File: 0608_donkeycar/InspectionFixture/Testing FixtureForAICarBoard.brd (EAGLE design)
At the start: 65 x 56.5 mm, 89 parts, among them CON1 RASPBERRYPI_SHEILD

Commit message: AI Car Board テスト治具 Rev1.0.0 アルファ版　完成
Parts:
- removed U$1: RP2350A, FaBo-MPU:QFN60
- removed U$10: MLP2520S2R2MT0S1, FaBo-Coil:1008(2520MM)
- removed U$11: DMG1012T, FaBo-Mosfet:SOT-523
- removed U$12, U$14: TS-06104, FaBo-Switch:TS-06104
- removed U$13: MCP3008, FaBo-ADC:SOIC-16
- removed U$2: W25Q32RVXHJQ, FaBo-NORFLASH:XSON8
- removed U$3: ABM8-272-T3, FaBo-Crystal:ABM8-272-T3
- removed U$5: TXB0104, FaBo-LevelTranslator:TSSOP-14
- removed U$6: PMEG6010ELR-Q, FaBo-Diode:SOD123W
- removed U$7: 5077CR-16-SMC2-BK-TR, FaBo-USB:5077CR-16-SMC2-BK-TR
- removed U$8: RT6150B-33GQW, FaBo-Supply:WDFN-10L_2.5X2.5MM
- removed U$9: AOTA-B201610S3R3-101-T, FaBo-Coil:0806(2016MM)
- added BT1, BT2: TS-06104, FaBo-Switch:TS-06104
- added C33: 0.1uF, FaBo-Capacitor:0603-BOTTOM
- added CN2, CN3, CN4, CN5, CN6: (no value), FaBo-PIN:PIN_1X1_SMALL
- added CON2: 5077CR-16-SMC2-BK-TR, FaBo-USB:5077CR-16-SMC2-BK-TR
- added D2, D3: PMEG6010ELR-Q, FaBo-Diode:SOD123W
- added L1: MLP2520S2R2MT0S1, FaBo-Coil:1008(2520MM)
- added L2: AOTA-B201610S3R3-101-T, FaBo-Coil:0806(2016MM)
- added LED2: (no value), FaBo-LED:WS2812B_NARROW
- added OSC: ABM8-272-T3, FaBo-Crystal:ABM8-272-T3
- added R38: 100K, FaBo-Resistors:0603
- added R39: DNP, FaBo-Resistors:0603-BOTTOM
- added U1: RP2350A, FaBo-MPU:QFN60
- added U3: TXB0104, FaBo-LevelTranslator:TSSOP-14
- added U4: RT6150B-33GQW, FaBo-Supply:WDFN-10L_2.5X2.5MM
- added U5: DMG1012T, FaBo-Mosfet:SOT-523
- added U6: MCP3008, FaBo-ADC:SOIC-16
- added U7: (no value), FaBo-Display:ER-CON30HT-1_REV2
- C10: value 47uF -> 10uF
- C11: value 1nF -> 0.1uF
- C12, C15, C16, C17, C18, C21: value 4.7uF -> 0.1uF
- C13: value 15pF -> 0.1uF
- C14: value 15pF -> 4.7uF
- C2: value 1uF -> 18pF
- C23, C25, C26, C27, C29: value 0.1uF -> 4.7uF
- C28: value 0.1uF -> 1nF
- C3: value 1uF -> 47uF
- C30, C31: value 0.1uF -> 15pF
- C6, C7: value 10uF -> 1uF
- C9: value 18pF -> 10uF
- R1, R2: value 10K -> 5.1K
- R10, R16, R20, R22, R23: value 100K -> 4.7K
- R11: value 4.7K -> DNP
- R12: value 5.6K -> DNP; device FaBo-Resistors:0603 -> FaBo-Resistors:0603-BOTTOM
- R13: value 4.7K -> 10K
- R14: value 10K -> 100; device FaBo-Resistors:0603 -> FaBo-Resistors:0603-BOTTOM
- R15: value 4.7K -> 390K
- R18: value 1K -> 4.7K
- R24, R25: value 100 -> DNP
- R26, R27: device FaBo-Resistors:0603 -> FaBo-Resistors:0603-BOTTOM
- R28, R35: value 10K -> 100K
- R29: value DNP -> 10K
- R30: value 470 -> DNP
- R31: value 4.7K -> 1K
- R32, R33: value DNP -> 100
- R34: value (none) -> 10K; device 52101-101-REV-A_v16:RC-MASTER-SMD_R1206MP -> FaBo-Resistors:0603-BOTTOM
- R36: value DNP -> 470
- R37: value DNP -> 100K; device FaBo-Resistors:0603-BOTTOM -> FaBo-Resistors:0603
- R4: value 390K -> 33
- R5: value 10K -> 5.6K; device FaBo-Resistors:0603-BOTTOM -> FaBo-Resistors:0603
- R6: value 100 -> 10K; device FaBo-Resistors:0603-BOTTOM -> FaBo-Resistors:0603
- R8: value 33 -> 100K
- U2: value (none) -> W25Q32RVXHJQ; device FaBo-Display:ER-CON30HT-1_REV2 -> FaBo-NORFLASH:XSON8
- moved R36 278.4 mm to (31.8, 24.2), flipped to the bottom, turned to 90 degrees
- moved R35 277.2 mm to (5.08, 30.7), turned to 90 degrees
- moved R37 275.1 mm to (11.3, 21.7)
- moved R33 268.1 mm to (54.4, 23.2), flipped to the bottom, turned to 90 degrees
- moved R13 262.4 mm to (55.4, 47.4)
- moved R32 261.9 mm to (54.6, 19.7), flipped to the bottom, turned to 270 degrees
- moved R15 261.2 mm to (54.1, 43.5), turned to 270 degrees
- moved R21 259.2 mm to (11.0, 42.9), flipped to the bottom, turned to 270 degrees
- moved R34 258.4 mm to (35.2, 15.6), flipped to the bottom
- moved R19 255.7 mm to (8.00, 42.9), flipped to the bottom, turned to 270 degrees
- moved R11 252.9 mm to (36.8, 46.2)
- moved R17 252.2 mm to (5.05, 42.8), flipped to the bottom, turned to 270 degrees
- moved C32 251.9 mm to (8.05, 23.8), flipped to the bottom, turned to 180 degrees
- moved R9 248.4 mm to (36.9, 44.6)
- moved C31 247.7 mm to (18.8, 20.7), flipped to the bottom, turned to 270 degrees
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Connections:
- removed net 3V3: C4.2, C5.2, CON1.1, CON1.17, D1.CATHODE, R5.2, U2.22, U2.25
- removed net N$29: R18.1, U$1.22
- removed net N$30: C14.2, U$1.21, U$3.3
- removed net N$31: U$1.48, U$9.1
- removed net N$32: R24.1, U$1.24
- removed net N$33: CN1.3, R25.2
- removed net N$35: U$13.13, U$5.13
- removed net N$36: CN1.1, R24.2
- removed net N$37: C17.2, R20.1, U$1.46
- removed net N$38: U$1.43, U$11.S
- removed net N$40: R28.1, R29.1, U$1.60, U$2.1
- removed net N$42: U$13.12, U$5.12
- removed net N$43: U$13.11, U$5.11
- removed net N$45: R30.2, U$1.37
- removed net N$46: U$13.10, U$5.10
- removed net N$47: R7.2, U$1.34, U$5.8
- removed net N$48: U$1.4, U$5.2
- removed net N$49: U$1.5, U$5.4
- removed net N$50: U$1.7, U$5.3
- removed net N$51: U$1.8, U$5.5
- removed net N$52: R9.2, U$13.1
- removed net N$53: R11.2, U$13.2
- removed net N$54: R13.2, U$13.3
- removed net N$55: R15.2, U$13.4
- removed net N$56: R17.2, U$13.5
- removed net N$57: R19.2, U$13.6
- removed net N$58: R21.2, U$13.7
- removed net N$59: R31.2, U$13.8
- removed net N$6: R8.1, U$7.A7:DN1, U$7.B7:DN2
- removed net N$60: CON1.3, R36.2
- removed net N$62: CON1.5, R37.2
- removed net N$67: R32.2, U$1.3
- removed net N$69: R33.2, U$1.2
- removed net N$8: R25.1, U$1.25
- removed net P-3V3: C10.2, C11.2, C12.2, C16.2, C19.2, C20.2, C24.2, C25.2, C26.2, C27.2, C28.2, R20.2, R22.2, R29.2, R35.2, U$1.1, U$1.11, U$1.20, U$1.30, U$1.38, U$1.45, U$1.49, U$1.53, U$1.54, U$11.G, U$2.8, U$8.1, U$8.10
- new net CLK: U3.13, U6.13
- new net CS: U3.10, U6.10
- new net DATA: CN1.3, R33.2
- new net DIN: U3.11, U6.11
- new net DOUT: U3.12, U6.12
- new net GP0: CN4.1, R24.2, U1.2
- new net GP1: CN5.1, R25.2, U1.3
- new net GP10: CN2.1, U1.14
- new net GP12: CN3.1, U1.16
- new net GP22: R35.2, U1.34, U3.8
- new net GP25: R36.2, R39.2, U1.37
- new net GPIO29: U1.43, U5.S
- new net MINUS: CON2.A7:DN1, CON2.B7:DN2, R3.1
- new net OSC-IN: C31.2, OSC.3, U1.21
- new net OSC-OUT: C30.2, OSC.1, R31.2
- new net PLUS: CON2.A6:DP1, CON2.B6:DP2, R4.1
- new net QSPI-CLK: U1.56, U2.6
- new net QSPI-SD0: U1.57, U2.5
- new net QSPI-SD1: U1.59, U2.2
- new net QSPI-SD2: U1.58, U2.3
- new net QSPI-SD3: U1.55, U2.7
- new net QSPI-SS: R29.1, R30.1, U1.60, U2.1
- new net SCL-PASPI: CON1.5, R12.2
- new net SDA-RASPI: CON1.3, R11.2
- new net SPI-RX: U1.7, U3.3
- new net SPI-SCLK: U1.4, U3.2
- new net SPI_CS: U1.8, U3.5
- new net SPI_TX: U1.5, U3.4
- new net SWCLK: R32.1, U1.24
- new net SWD: R33.1, U1.25
- new net SW_CLK: CN1.1, R32.2
- new net VRGE_AVDD: C25.2, R28.1, U1.46
- new net VRGE_LV: L2.1, U1.48
- new net VSYS_3V3: C15.2, C16.2, C17.2, C18.2, C19.2, C20.2, C21.2, C27.2, C28.2, C29.2, C3.2, C6.2, C7.2, D1.CATHODE, R10.2, R13.2, R26.2, R28.2, R30.2, R34.2, R9.2, U1.1, U1.11, U1.20, U1.30, U1.38, U1.45, U1.49, U1.53, U1.54, U2.8, U4.1, U4.10, U5.G, U7.22, U7.25
- new net XOUT: R31.1, U1.22
- net 1V1: now also C24.2, C26.2, L2.2, U1.23, U1.39, U1.50, U1.6; no longer C15.2, C21.2, U$1.23, U$1.39, U$1.50, U$1.6, U$9.2
- net 5V: now also D3.2; no longer CON3.VCC, R34.1
- net ADC-VREF: now also R26.1, R27.2; no longer R22.1, R23.2
- net GND: now also BT1.A, BT1.B, BT2.C, BT2.D, C2.1, C3.1, C33.1, CN6.1, CON2.A1,B12:GND, CON2.B1,A12:GND, CON2.SHILED1, CON2.SHILED2, CON2.SHILED3, CON2.SHILED4, CON2.SHILED5, CON2.SHILED6, CON2.SHILED7, CON2.SHILED8, LED2.3-VSS, OSC.2, OSC.4, R1.2, R15.1, R2.2, R35.1, R38.1, R6.1, R8.1, U1.47, U1.61, U1.P$62, U1.P$63, U1.P$64, U1.P$65, U1.P$66, U1.P$67, U1.P$68, U1.P$69, U1.P$70, U2.4, U3.7, U4.3, U4.9, U4.PAD, U6.14, U6.9, U7.10, U7.14, U7.15, U7.16, U7.18, U7.19, U7.2, U7.21, U7.23, U7.6, U7.7, U7.8, U7.9; no longer C4.1, C5.1, R14.1, R16.1, R27.1, R4.1, R7.1, U$1.47, U$1.61, U$1.P$62, U$1.P$63, U$1.P$64, U$1.P$65, U$1.P$66, U$1.P$67, U$1.P$68, U$1.P$69, U$1.P$70, U$12.A, U$12.B, U$13.14, U$13.9, U$14.C, U$14.D, U$2.4, U$2.9, U$3.2, U$3.4, U$5.7, U$7.A1,B12:GND, U$7.B1,A12:GND, U$7.SHILED1, U$7.SHILED2, U$7.SHILED3, U$7.SHILED4, U$7.SHILED5, U$7.SHILED6, U$7.SHILED7, U$7.SHILED8, U$8.3, U$8.9, U$8.PAD, U2.10, U2.14, U2.15, U2.16, U2.18, U2.19, U2.2, U2.21, U2.23, U2.6, U2.7, U2.8
- net GPIO23: now also R8.2, U1.35, U4.7; no longer R16.2, U$1.35, U$8.7
- net GPIO24: now also R5.1, R6.2, U1.36; no longer U$1.36
- net N$1: now also CON2.A5:CC1; no longer U$7.A5:CC1
- net N$10: now also L1.1, U4.4; no longer U$10.1, U$8.4
- net N$11: now also L1.2, U4.2; no longer U$10.2, U$8.2
- net N$12: now also R7.1, U4.6; no longer R10.1, U$8.6
- net N$13: now also R22.2, U6.2; no longer R12.1, R14.2
- net N$14: now also C4.2, U7.27; no longer C2.2, U2.27
- net N$16: now also R21.2, U6.3; no longer U$1.56, U$2.6
- net N$17: now also R20.2, U6.4; no longer U$1.57, U$2.5
- net N$18: now also R19.2, U6.5; no longer U$1.59, U$2.2
- net N$19: now also C5.1, U7.28; no longer C3.1, U2.28
- net N$2: now also CON2.B5:CC2; no longer U$7.B5:CC2
- net N$20: now also R18.2, U6.6; no longer U$1.58, U$2.3
- net N$21: now also C5.2, U7.29; no longer C3.2, U2.29
- net N$22: now also R17.2, U6.7; no longer U$1.55, U$2.7
- net N$23: now also R15.2, U7.5; no longer R4.2, U2.5
- net N$24: now also C8.2, U7.4; no longer C6.2, U2.4
- net N$25: now also C9.2, U7.3; no longer C7.2, U2.3
- net N$26: now also R14.1, U7.17, U7.20; no longer R6.1, U2.17, U2.20
- net N$27: now also C10.2, R13.1, R14.2; no longer C8.2, R5.1, R6.2
- net N$28: now also R16.2, U6.8; no longer C13.2, R18.2, U$3.1
- net N$3: now also LED2.4-DIN, R39.1; no longer R1.2, R2.2
- net N$34: now also C14.2, R27.1, U1.44; no longer C18.2, R23.1, U$1.44
- net N$39: now also C32.2, R37.1, R38.2, U5.D; no longer C29.2, R26.1, R27.2, U$11.D
- net N$4: now also CON2.A8:SBU1; no longer U$7.A8:SBU1
- net N$41: now also BT1.C, BT1.D, R29.2; no longer R28.2, U$12.C, U$12.D
- net N$44: now also R36.1; no longer R30.1
- net N$5: now also CON2.B8:SBU2; no longer U$7.B8:SBU2
- net N$61: now also C13.2, U3.1; no longer C31.2, U$5.1
- net N$7: now also C4.1, U7.26; no longer C2.1, U2.26
- net N$9: now also R23.2, U6.1; no longer R3.1, U$7.A6:DP1, U$7.B6:DP2
- net PIN11: now also R16.1; no longer R9.1
- net PIN13: now also R17.1; no longer R11.1
- net PIN15: now also R18.1; no longer R13.1
- net PIN29: now also R19.1; no longer R15.1
- net PIN31: now also R20.1; no longer R17.1
- net PIN33: now also R21.1; no longer R19.1
- net PIN35: now also R22.1; no longer R21.1
- net PIN37: now also R23.1; no longer R31.1
- net RUN: now also BT2.A, BT2.B, R34.1, U1.26; no longer R35.1, U$1.26, U$14.A, U$14.B
- net SCL: now also R10.1, R12.1, U1.28, U7.13; no longer R37.1, U$1.28, U2.13
- net SDA: now also R11.1, R9.1, U1.27, U7.11, U7.12; no longer R36.1, U$1.27, U2.11, U2.12
- net UNDER: now also R25.1; no longer R32.1
- net UPWARD: now also R24.1; no longer R33.1
- net USB_DM: now also R3.2, U1.51; no longer R8.2, U$1.51
- net USB_DP: now also C2.2, R4.2, U1.52; no longer C9.2, R3.2, U$1.52
- net VBUS: now also CON2.A4,B9:VBUS, CON2.B4,A9:VBUS, D2.2, R5.2; no longer R12.2, U$6.1, U$7.A4,B9:VBUS, U$7.B4,A9:VBUS
- net VSYS: now also C11.2, C12.2, C33.2, CON3.VCC, D2.1, D3.1, LED2.1-VDD, R37.2, R7.2, U3.14, U4.5, U4.8, U6.15, U6.16; no longer C30.2, C32.2, R10.2, R26.2, R34.2, U$13.15, U$13.16, U$5.14, U$6.2, U$8.5, U$8.8
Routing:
- net GND: track 233.9 -> 744.4 mm, vias 28 -> 79
- net VSYS_3V3: track 0.00 -> 246.9 mm, vias 0 -> 14
- net VSYS: track 0.00 -> 150.0 mm, vias 0 -> 11
- net 3V3: track 120.0 -> 0.00 mm, vias 4 -> 0
- net SDA: track 9.72 -> 119.0 mm, vias 1 -> 5
- net GP22: track 0.00 -> 92.7 mm, vias 0 -> 4
- net SCL: track 7.90 -> 98.5 mm
- net GP25: track 0.00 -> 70.0 mm, vias 0 -> 4
- net SWCLK: track 0.00 -> 55.3 mm, vias 0 -> 2
- net GPIO29: track 0.00 -> 54.9 mm, vias 0 -> 4
- net SWD: track 0.00 -> 54.2 mm, vias 0 -> 2
- net 1V1: track 0.00 -> 52.8 mm, vias 0 -> 5
- net MINUS: track 0.00 -> 44.7 mm
- net PLUS: track 0.00 -> 44.1 mm
- net QSPI-SS: track 0.00 -> 40.9 mm, vias 0 -> 2
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- added copper zone on layer 1, net 1V1
- added copper zone on layer 16, net 1V1
- added copper zone on layer 1, net VBUS
- added copper zone on layer 16, net VBUS
- added copper zone on layer 1, net VSYS
- added copper zone on layer 16, net VSYS
- added copper zone on layer 1, net VSYS_3V3
- added copper zone on layer 16, net VSYS_3V3
- added copper zone on layer 16, net ５V
- removed copper zone on layer 1, net 3V3
- removed copper zone on layer 16, net 3V3
- removed copper zone on layer 1, net 5V
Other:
- board text added: "BOOT"
- board text added: "CLK"
- board text added: "DATA"
- board text added: "GP0"
- board text added: "GP1"
- board text added: "MCP3008"
- board text added: "RESET"
- board text added: "RP2350A"
- board text added: "RT6150"
- board text added: "Rev1.0.0"
- board text added: "SWD"
- board text added: "TXB0104PW"
- board text added: "Testing Jig For AI Car Board Rev1.0.0 2025/03/31 DKFA-JIG-01"
- board text added: "VSYS"
- board text added: "W25Q32"
- board text removed: "5V"
- board text removed: "FaBo AI Car Board"
- board text removed: "Testing Jig For AI Car Board Rev1.0.0 2025/03/27 DKFA-JIG-01"

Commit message: AI Car Board べた修正。
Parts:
- moved CN4 0.54 mm to (27.9, 48.6)
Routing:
- net GP0: track 32.4 -> 32.9 mm
- added copper zone on layer 1, net 5V
- added copper zone on layer 16, net 5V
- removed copper zone on layer 16, net ５V
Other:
- board text added: "AI Car Board TEST"
- board text added: "Testing Jig For AI Car Board Rev1.0.0 2025/04/02 DKFA-JIG-01"
- board text removed: "Testing Jig For AI Car Board Rev1.0.0 2025/03/31 DKFA-JIG-01"
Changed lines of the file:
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@@
 <wire x1="52.51" y1="39.942" x2="52.51" y2="38.142" width="0.03" layer="42"/>
 <text x="2.7220875" y="-18.00531875" size="2.54" layer="48" font="vector" ratio="15">Testing Jig For AI Car Board
-Rev1.0.0 2025/03/31
+Rev1.0.0 2025/04/02
 DKFA-JIG-01</text>
 <text x="57.3132375" y="36.539034375" size="1.27" layer="125" font="vector" ratio="15" align="bottom-right">0.96inch OLED</text>
@@
 <text x="59.6138" y="20.5232" size="0.508" layer="21" font="vector" ratio="12" rot="R270" align="center">GND</text>
 <text x="59.6138" y="23.0632" size="0.508" layer="21" font="vector" ratio="12" rot="R270" align="center">DATA</text>
+<text x="31.398090625" y="5.410459375" size="1.524" layer="21" font="vector" ratio="15" rot="R180" align="bottom-center">AI Car Board
+TEST</text>
 </plain>
 <attributes>
@@
 <element name="CN2" library="FaBo-PIN" package="PIN_1X1_SMALL" value="" x="16.383" y="23.2156" smashed="yes"/>
 <element name="CN3" library="FaBo-PIN" package="PIN_1X1_SMALL" value="" x="19.2786" y="24.638" smashed="yes"/>
-<element name="CN4" library="FaBo-PIN" package="PIN_1X1_SMALL" value="" x="27.5082" y="48.2346" smashed="yes"/>
+<element name="CN4" library="FaBo-PIN" package="PIN_1X1_SMALL" value="" x="27.8892" y="48.6156" smashed="yes"/>
 <element name="CN5" library="FaBo-PIN" package="PIN_1X1_SMALL" value="" x="3.048" y="37.1094" smashed="yes"/>
 <element name="LED2" library="FaBo-LED" package="WS2812B_NARROW" value="" x="49.7586" y="18.8976" smashed="yes">
@@
 <wire x1="4.9022" y1="24.31" x2="4.9022" y2="26.162" width="0.3048" layer="1"/>
 <wire x1="4.9022" y1="26.162" x2="4.8514" y2="26.2128" width="0.1524" layer="1"/>
+<polygon width="0.1524" layer="1" thermals="no">
+<vertex x="2.159" y="26.035"/>
+<vertex x="2.159" y="28.575"/>
+<vertex x="3.048" y="29.464"/>
+<vertex x="4.191" y="29.464"/>
+<vertex x="5.588" y="28.067"/>
+<vertex x="5.842" y="27.813"/>
+<vertex x="5.842" y="26.289"/>
+<vertex x="5.842" y="26.162"/>
+<vertex x="5.461" y="25.781"/>
+<vertex x="5.461" y="24.003"/>
+<vertex x="5.334" y="23.876"/>
+<vertex x="3.81" y="23.876"/>
+<vertex x="3.683" y="24.003"/>
+<vertex x="2.159" y="25.527"/>
+</polygon>
+<polygon width="0.1524" layer="16" thermals="no">
+<vertex x="2.3876" y="26.2382"/>
+<vertex x="2.3876" y="28.4226"/>
+<vertex x="3.4036" y="29.4386"/>
+<vertex x="3.7846" y="29.4386"/>
+<vertex x="5.461" y="27.7622"/>
+<vertex x="5.461" y="24.6888"/>
+<vertex x="4.699" y="23.9268"/>
+</polygon>
 </signal>
 <signal name="SDA">
@@
 <contactref element="CN4" pad="1"/>
 <wire x1="18.8976" y1="46.267" x2="25.5406" y2="46.267" width="0.1524" layer="16"/>
-<wire x1="25.5406" y1="46.267" x2="27.5082" y2="48.2346" width="0.1524" layer="16"/>
+<wire x1="25.5406" y1="46.267" x2="27.8892" y2="48.6156" width="0.1524" layer="16"/>
 </signal>
 <signal name="GP1">
@@
 <wire x1="4.5644" y1="39.3776" x2="3.5306" y2="40.4114" width="0.1524" layer="1"/>
 </signal>
-<signal name="５V">
-<polygon width="0.1524" layer="16" thermals="no">
-<vertex x="2.3876" y="27.0256"/>
-<vertex x="2.3876" y="28.4226"/>
-<vertex x="3.4036" y="29.4386"/>
-<vertex x="3.7846" y="29.4386"/>
-<vertex x="5.461" y="27.7622"/>
-<vertex x="5.461" y="24.6888"/>
-<vertex x="4.826" y="24.0538"/>
-<vertex x="2.3876" y="26.4922"/>
-</polygon>
-</signal>
 <signal name="N$3">

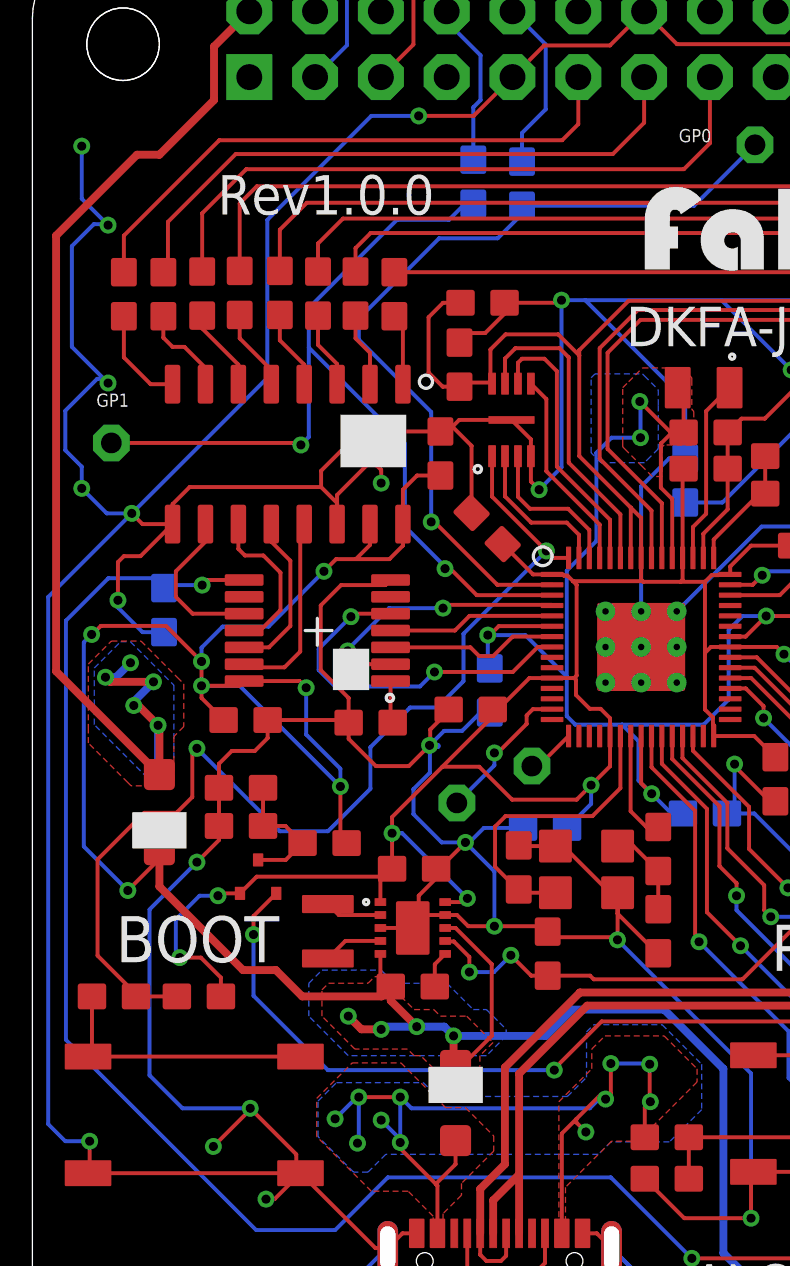
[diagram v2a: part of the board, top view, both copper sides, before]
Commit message: #608 AI Car Board InspectionBoard　C34コンデンサ47uF追加修正。
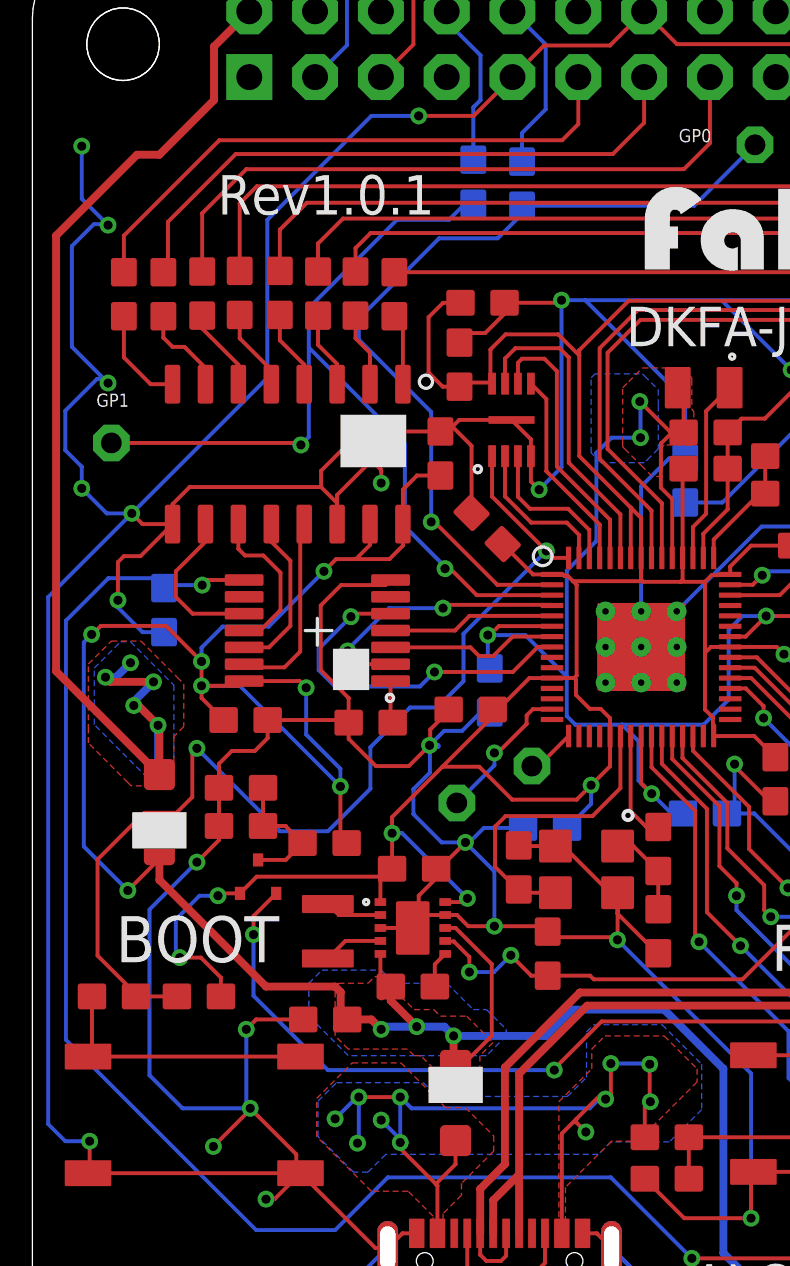
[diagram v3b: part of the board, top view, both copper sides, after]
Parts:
- added C34: 47uF, FaBo-Capacitor:0603-BOTTOM
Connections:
- net GND: now also C34.1
- net VSYS: now also C34.2
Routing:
- net GND: track 744.4 -> 749.8 mm, vias 79 -> 80
- net VSYS: track 150.0 -> 149.3 mm, vias 11 -> 10
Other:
- board text added: "5077CR-16-SMC2-BK-TR"
- board text added: "Rev1.0.1"
- board text added: "TS-06104"
- board text added: "Testing Jig For AI Car Board Rev1.0.1 2025/04/17 DKFA-JIG-01"
- board text removed: "Rev1.0.0"
- board text removed: "Testing Jig For AI Car Board Rev1.0.0 2025/04/02 DKFA-JIG-01"
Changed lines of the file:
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@@
 <drawing>
 <settings>
-<setting alwaysvectorfont="yes"/>
+<setting alwaysvectorfont="no"/>
 <setting keepoldvectorfont="yes"/>
 <setting verticaltext="up"/>
@@
 <wire x1="52.51" y1="39.942" x2="52.51" y2="38.142" width="0.03" layer="42"/>
 <text x="2.7220875" y="-18.00531875" size="2.54" layer="48" font="vector" ratio="15">Testing Jig For AI Car Board
-Rev1.0.0 2025/04/02
+Rev1.0.1 2025/04/17
 DKFA-JIG-01</text>
 <text x="57.3132375" y="36.539034375" size="1.27" layer="125" font="vector" ratio="15" align="bottom-right">0.96inch OLED</text>
@@
 <text x="25.5778" y="48.9712" size="0.508" layer="21" font="vector" ratio="12" rot="R180" align="center">GP0</text>
 <text x="3.0988" y="38.7604" size="0.508" layer="21" font="vector" ratio="12" rot="R180" align="center">GP1</text>
-<text x="11.332090625" y="47.447459375" size="1.524" layer="21" font="vector" ratio="15" rot="R180" align="bottom-center">Rev1.0.0</text>
+<text x="11.332090625" y="47.447459375" size="1.524" layer="21" font="vector" ratio="15" rot="R180" align="bottom-center">Rev1.0.1</text>
 <text x="35.8648" y="5.2832" size="0.508" layer="21" font="vector" ratio="12" rot="R180" align="center">GND</text>
 <text x="59.7408" y="18.1102" size="0.508" layer="21" font="vector" ratio="12" rot="R270" align="center">CLK</text>
@@
 <text x="31.398090625" y="5.410459375" size="1.524" layer="21" font="vector" ratio="15" rot="R180" align="bottom-center">AI Car Board
 TEST</text>
+<circle x="22.987" y="22.733" radius="0.179603125" width="0.1524" layer="21"/>
+<text x="7.561721875" y="3.290525" size="1.27" layer="125" font="vector" ratio="15" rot="R180" align="bottom-right">5077CR-16-SMC2-BK-TR</text>
+<text x="1.719721875" y="12.053525" size="1.27" layer="125" font="vector" ratio="15" rot="R180" align="bottom-right">TS-06104</text>
+<text x="27.246721875" y="11.926525" size="1.27" layer="125" font="vector" ratio="15" rot="R180" align="bottom-right">TS-06104</text>
 </plain>
 <attributes>
@@
 </element>
 <element name="CN6" library="FaBo-PIN" package="PIN_1X1_SMALL" value="" x="35.814" y="4.064" smashed="yes"/>
+<element name="C34" library="FaBo-Capacitor" package="0603-BOTTOM" value="47uF" x="11.303" y="14.859" smashed="yes" rot="MR180">
+<attribute name="NAME" x="11.303" y="13.97" size="0.8128" layer="125" font="vector" ratio="12" rot="MR180" align="bottom-center"/>
+<attribute name="SPICEPREFIX" value="C" x="11.303" y="14.859" size="1.778" layer="28" rot="MR180" display="off"/>
+<attribute name="VALUE" x="11.049" y="15.875" size="0.8128" layer="27" font="vector" ratio="12" rot="MR180" align="center"/>
+</element>
 </elements>
 <signals>
@@
 <wire x1="4.5212" y1="19.1008" x2="4.5212" y2="12.7" width="0.1524" layer="16"/>
 <wire x1="4.5212" y1="12.7" x2="5.7912" y2="11.43" width="0.1524" layer="16"/>
-<wire x1="5.7912" y1="11.43" x2="8.4074" y2="11.43" width="0.1524" layer="16"/>
+<wire x1="5.7912" y1="11.43" x2="8.255" y2="11.43" width="0.1524" layer="16"/>
 <via x="8.4074" y="11.43" extent="1-16" drill="0.35"/>
+<wire x1="8.255" y1="11.43" x2="8.4074" y2="11.43" width="0.1524" layer="16"/>
 <wire x1="8.4074" y1="11.43" x2="10.1854" y2="9.652" width="0.1524" layer="1"/>
 <wire x1="10.1854" y1="9.652" x2="10.1854" y2="8.926" width="0.1524" layer="1"/>
@@
 <wire x1="62.1792" y1="35.7378" x2="62.1792" y2="37.0078" width="0.1524" layer="16"/>
 <wire x1="62.1792" y1="37.0078" x2="63.6524" y2="38.481" width="0.1524" layer="16"/>
+<contactref element="C34" pad="1"/>
+<wire x1="10.453" y1="14.859" x2="8.636" y2="14.859" width="0.1524" layer="1"/>
+<wire x1="8.636" y1="14.859" x2="8.255" y2="14.478" width="0.1524" layer="1"/>
+<via x="8.255" y="14.478" extent="1-16" drill="0.35"/>
+<wire x1="8.255" y1="14.478" x2="8.255" y2="11.43" width="0.1524" layer="16"/>
 </signal>
 <signal name="5V">
@@
 <wire x1="49.1372" y1="18.919" x2="47.5086" y2="20.5476" width="0.1524" layer="1"/>
 <contactref element="CON3" pad="VCC"/>
-<wire x1="4.9022" y1="21.41" x2="4.9022" y2="19.9898" width="0.3048" layer="1"/>
-<wire x1="9.398" y1="16.764" x2="10.414" y2="15.748" width="0.3048" layer="1"/>
-<wire x1="10.414" y1="15.748" x2="13.4756" y2="15.748" width="0.3048" layer="1"/>
+<wire x1="4.9022" y1="21.41" x2="4.9022" y2="20.2438" width="0.3048" layer="1"/>
 <wire x1="13.4756" y1="15.748" x2="13.8312" y2="16.1036" width="0.3048" layer="1"/>
-<wire x1="4.9022" y1="19.9898" x2="8.128" y2="16.764" width="0.3048" layer="1"/>
-<wire x1="8.128" y1="16.764" x2="9.398" y2="16.764" width="0.3048" layer="1"/>
 <wire x1="14.8347" y1="14.5807" x2="13.8312" y2="15.5842" width="0.3048" layer="1"/>
 <wire x1="13.8312" y1="15.5842" x2="13.8312" y2="16.1036" width="0.3048" layer="1"/>
@@
 <wire x1="13.5647" y1="14.5807" x2="13.462" y2="14.478" width="0.3048" layer="16"/>
 <via x="13.462" y="14.478" extent="1-16" drill="0.35"/>
-<wire x1="13.462" y1="14.478" x2="12.7" y2="14.478" width="0.3048" layer="1"/>
-<wire x1="12.7" y1="14.478" x2="12.192" y2="14.986" width="0.3048" layer="1"/>
-<via x="12.192" y="14.986" extent="1-16" drill="0.35"/>
 <wire x1="16.256" y1="14.224" x2="19.812" y2="14.224" width="0.3048" layer="16"/>
 <wire x1="19.812" y1="14.224" x2="20.828" y2="15.24" width="0.3048" layer="16"/>
@@
 <wire x1="49.1372" y1="14.3628" x2="50.292" y2="13.208" width="0.3048" layer="1"/>
 <polygon width="0.1524" layer="1" thermals="no">
-<vertex x="11.176" y="16.002"/>
-<vertex x="11.43" y="16.256"/>
+<vertex x="11.684" y="16.129"/>
+<vertex x="11.811" y="16.256"/>
 <vertex x="12.954" y="16.256"/>
 <vertex x="13.208" y="16.51"/>
@@
 <vertex x="14.732" y="13.462"/>
 <vertex x="14.478" y="13.716"/>
-<vertex x="12.446" y="13.716"/>
-<vertex x="11.176" y="14.986"/>
+<vertex x="12.192" y="13.716"/>
+<vertex x="11.684" y="14.224"/>
 </polygon>
 <polygon width="0.1524" layer="16" thermals="no">
@@
 <vertex x="12.192" y="13.462"/>
 </polygon>
+<contactref element="C34" pad="2"/>
+<wire x1="11.899" y1="15.914" x2="11.899" y2="15.113" width="0.3048" layer="1"/>
+<wire x1="11.899" y1="15.113" x2="12.153" y2="14.859" width="0.3048" layer="1"/>
+<wire x1="4.9022" y1="20.2438" x2="9.017" y2="16.129" width="0.3048" layer="1"/>
+<wire x1="9.017" y1="16.129" x2="11.684" y2="16.129" width="0.3048" layer="1"/>
+<wire x1="11.684" y1="16.129" x2="11.899" y2="15.914" width="0.3048" layer="1"/>
+<wire x1="12.153" y1="14.859" x2="13.081" y2="14.859" width="0.3048" layer="1"/>
+<wire x1="13.081" y1="14.859" x2="13.462" y2="14.478" width="0.3048" layer="1"/>
 </signal>
 <signal name="N$10">
